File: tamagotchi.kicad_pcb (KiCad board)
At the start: 2 copper layers, 60.8 x 77.1 mm, 10 parts, among them SW1 SW_Push, SW2 SW_Push, SW3 SW_Push, U1 XIAO-ESP32-C3-SMD, U2 HS96L03W2C03

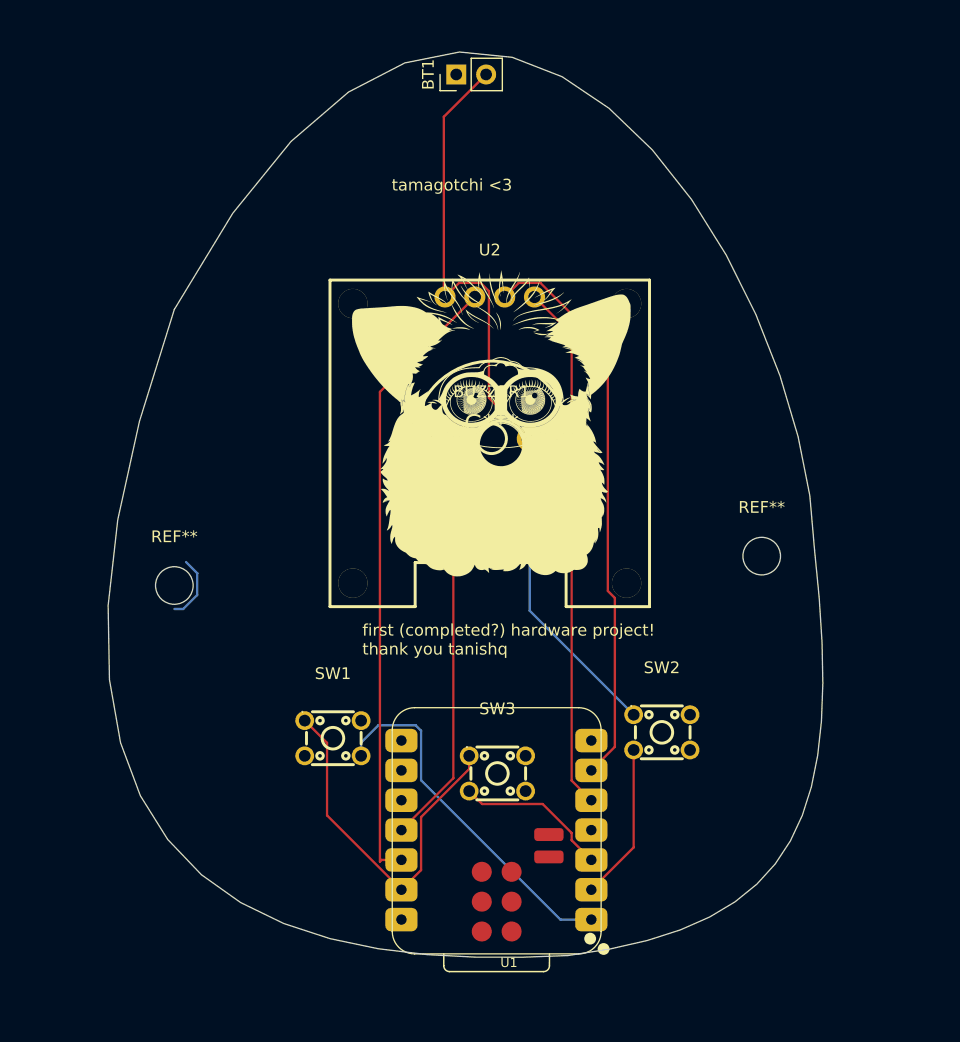
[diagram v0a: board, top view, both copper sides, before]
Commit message: finished routing and fixed DRC errors
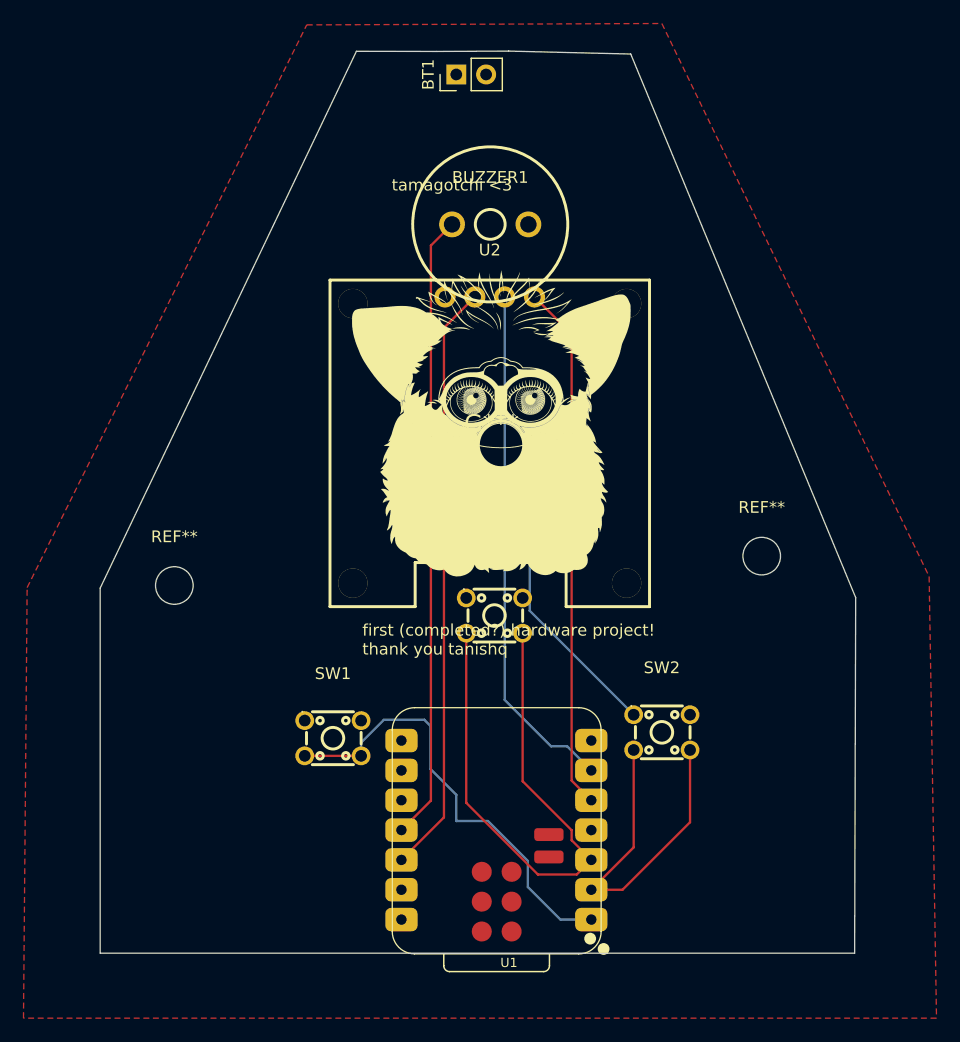
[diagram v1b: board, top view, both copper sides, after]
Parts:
- moved BUZZER1 18.2 mm to (71.9, 54.3)
- moved SW3 13.4 mm to (72.2, 87.6)
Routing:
- net GND: track 97.8 -> 27.3 mm
- net Net-(U1-GPIO4_A2_D2): track 13.2 -> 49.8 mm
- net Net-(BUZZER1-+): track 35.2 -> 53.3 mm
- net Net-(U1-GPIO3_A1_D1): track 13.4 -> 30.3 mm
- net Net-(U1-GPIO2_A0_D0): track 30.7 -> 38.1 mm
- net (no net): track 5.65 -> 0.00 mm
- net Net-(U1-GPIO7_D5_SCL): track 48.5 -> 44.2 mm
- net +3V3: track 53.3 -> 50.5 mm
- added copper zone on F.Cu, net GND
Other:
- board size 60.8 x 77.1 mm -> 64.3 x 76.8 mm

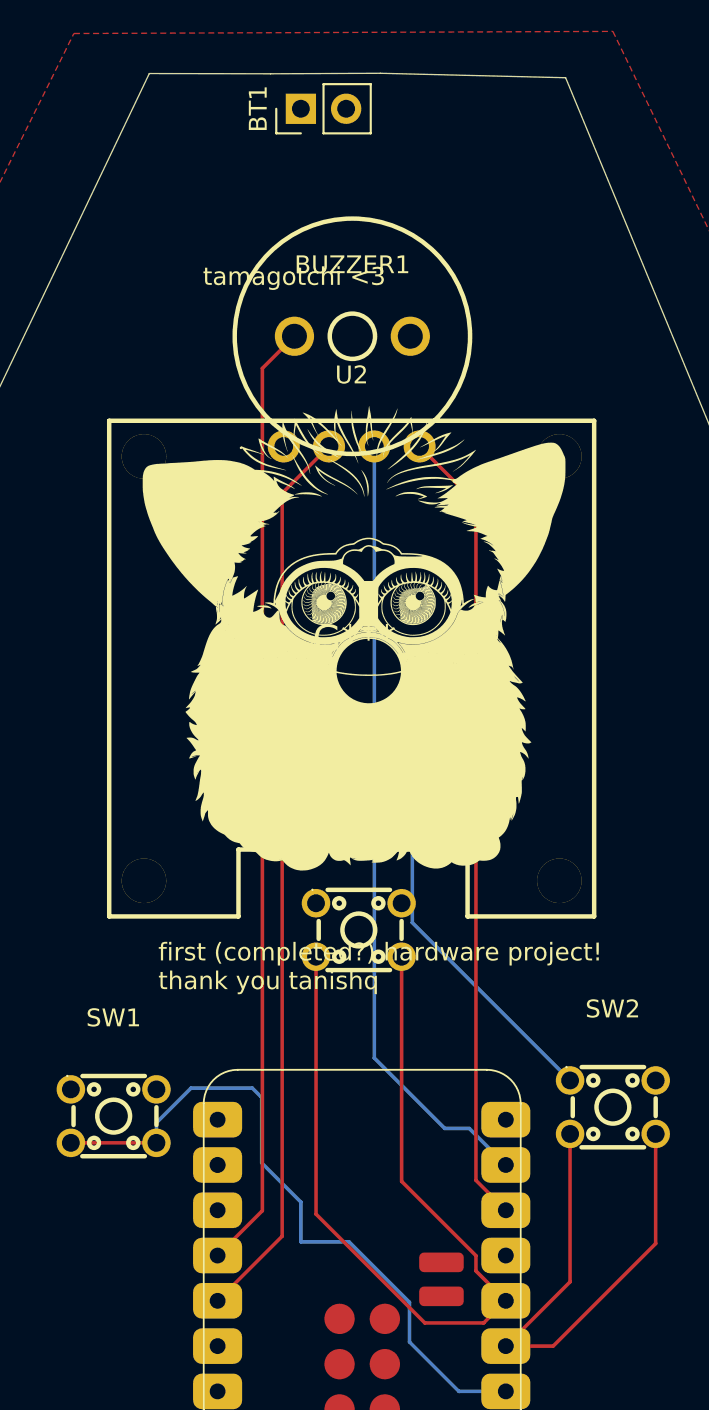
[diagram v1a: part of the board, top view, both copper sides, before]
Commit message: fixed up some really dumb xiao-esp32 issues (namely with the button numbers being wrong
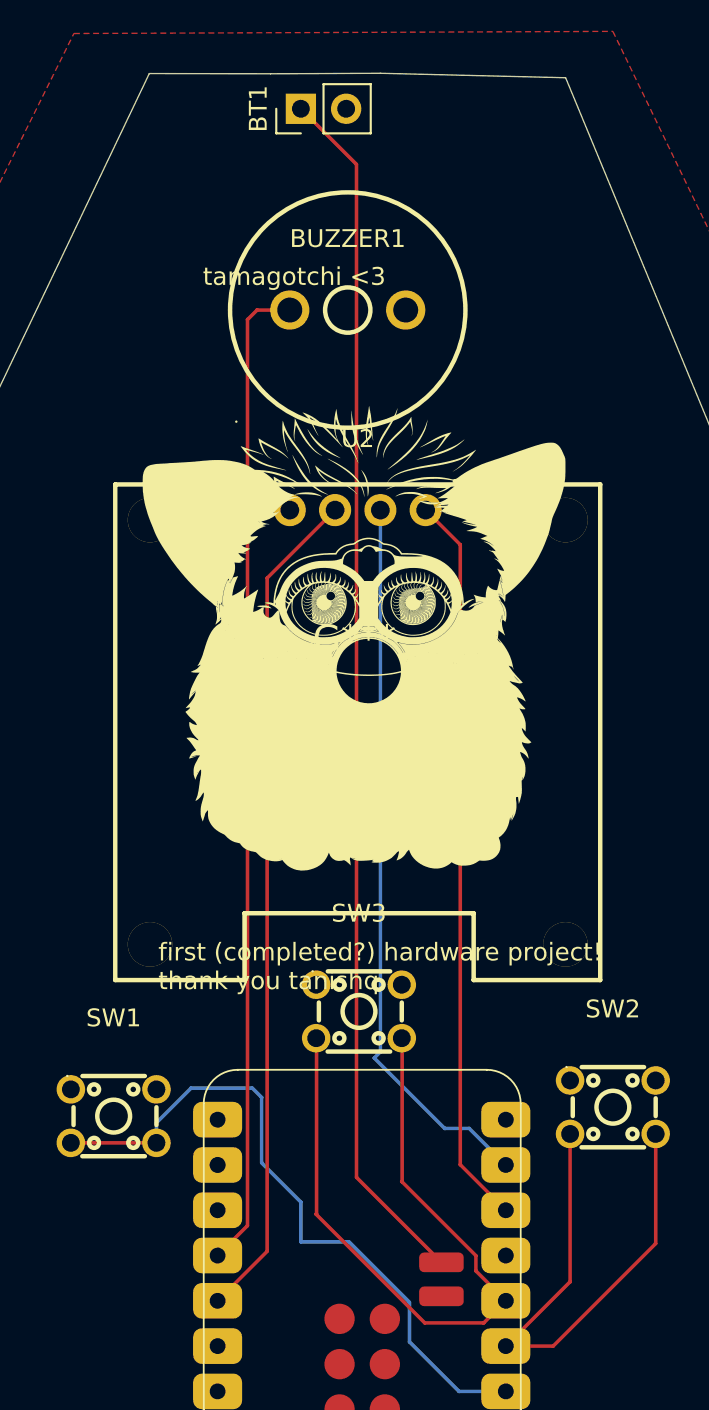
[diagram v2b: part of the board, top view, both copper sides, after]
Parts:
- moved SW3 4.57 mm to (72.3, 92.1)
- moved U2 3.59 mm to (72.2, 64.0)
- moved BUZZER1 1.49 mm to (71.6, 52.8)
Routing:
- net +BATT: track 0.00 -> 68.0 mm
- net GND: track 27.3 -> 0.00 mm
- net Net-(U1-GPIO4_A2_D2): track 49.8 -> 39.6 mm
- net Net-(U1-GPIO6_D4_SDA): track 44.8 -> 41.1 mm
- net Net-(U1-GPIO7_D5_SCL): track 44.2 -> 40.7 mm
- net +3V3: track 50.5 -> 47.1 mm
- net Net-(BUZZER1-+): track 53.3 -> 55.8 mm
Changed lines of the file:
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@@
 			(thermal_bridge_angle 45)
 		)
-		(pad "15" smd roundrect
-			(at 4.445 -10.882)
-			(size 2.5 1.1)
-			(layers "F.Cu" "F.Mask" "F.Paste")
-			(roundrect_rratio 0.25)
-			(thermal_bridge_angle 45)
-		)
-		(pad "16" smd roundrect
-			(at 4.445 -12.787)
-			(size 2.5 1.1)
-			(layers "F.Cu" "F.Mask" "F.Paste")
-			(roundrect_rratio 0.25)
-			(thermal_bridge_angle 45)
-		)
-		(pad "17" smd circle
+		(pad "24" smd circle
 			(at 7.62 -19.132 180)
 			(size 1.7 1.7)
 			(layers "F.Cu" "F.Mask" "F.Paste")
+			(net "unconnected-(U1-GPIO5_MTDI-Pad24)")
+			(pinfunction "GPIO5_MTDI_24")
+			(pintype "passive+no_connect")
 		)
-		(pad "18" smd circle
+		(pad "25" smd circle
 			(at 10.16 -19.132 180)
 			(size 1.7 1.7)
 			(layers "F.Cu" "F.Mask" "F.Paste")
+			(net "unconnected-(U1-GPIO7_MTDO-Pad25)")
+			(pinfunction "GPIO7_MTDO_25")
+			(pintype "passive+no_connect")
 		)
-		(pad "19" smd circle
+		(pad "26" smd circle
 			(at 7.62 -16.592 180)
 			(size 1.7 1.7)
 			(layers "F.Cu" "F.Mask" "F.Paste")
+			(net "unconnected-(U1-CHIP_EN-Pad26)")
+			(pinfunction "CHIP_EN_26")
+			(pintype "passive+no_connect")
 		)
-		(pad "20" smd circle
+		(pad "27" smd circle
 			(at 10.16 -16.592 180)
 			(size 1.7 1.7)
 			(layers "F.Cu" "F.Mask" "F.Paste")
+			(net "unconnected-(U1-GND-Pad27)")
+			(pinfunction "GND_27")
+			(pintype "passive+no_connect")
 		)
-		(pad "21" smd circle
+		(pad "28" smd circle
 			(at 7.62 -14.052 180)
 			(size 1.7 1.7)
 			(layers "F.Cu" "F.Mask" "F.Paste")
+			(net "unconnected-(U1-GPIO4_MTMS-Pad28)")
+			(pinfunction "GPIO4_MTMS_28")
+			(pintype "passive+no_connect")
 		)
-		(pad "22" smd circle
+		(pad "29" smd circle
 			(at 10.16 -14.052 180)
 			(size 1.7 1.7)
 			(layers "F.Cu" "F.Mask" "F.Paste")
+			(net "unconnected-(U1-GPIO6_MTCK-Pad29)")
+			(pinfunction "GPIO6_MTCK_29")
+			(pintype "passive+no_connect")
+		)
+		(pad "32" smd roundrect
+			(at 4.445 -10.882)
+			(size 2.5 1.1)
+			(layers "F.Cu" "F.Mask" "F.Paste")
+			(roundrect_rratio 0.25)
+			(net "+BATT")
+			(pinfunction "BAT_32")
+			(pintype "passive")
+			(thermal_bridge_angle 45)
+		)
+		(pad "33" smd roundrect
+			(at 4.445 -12.787)
+			(size 2.5 1.1)
+			(layers "F.Cu" "F.Mask" "F.Paste")
+			(roundrect_rratio 0.25)
+			(net "GND")
+			(pinfunction "GND_33")
+			(pintype "passive")
+			(thermal_bridge_angle 45)
 		)
 		(embedded_fonts no)
@@
 	(footprint "easyeda2kicad:SW-TH_4P-L4.5-W4.5-P3.00-LS4.8"
 		(layer "F.Cu")
-		(at 72.25 87.56)
+		(at 72.26 92.13)
 		(property "Reference" "SW3"
 			(at 0 -5.5 0)
@@
 	(footprint "easyeda2kicad:BUZ-TH_BD12.5-P6.50-D1.4"
 		(layer "F.Cu")
-		(at 71.89 54.26)
+		(at 71.62946 52.789706)
 		(property "Reference" "BUZZER1"
 			(at 0 -4 0)
@@
 			(layer "F.SilkS")
 		)
-		(fp_line
-			(start -6.25 0)
-			(end 6.25 0)
-			(stroke
-				(width 0.05)
-				(type solid)
-			)
-			(layer "F.CrtYd")
-		)
-		(fp_line
-			(start 6.25 0)
-			(end -6.25 0)
+		(fp_rect
+			(start -9.96025 -7.5435)
+			(end 9.481331 7.524089)
 			(stroke
 				(width 0.05)
-				(type solid)
+				(type default)
 			)
+			(fill no)
 			(layer "F.CrtYd")
 		)
@@
 	(footprint "easyeda2kicad:OLED-TH_L27.8-W27.2-P2.54_C9900033791"
 		(layer "F.Cu")
-		(at 71.85 60.44)
+		(at 72.19 64.01)
 		(property "Reference" "U2"
 			(at 0 -4 0)
@@
 		(layer "Edge.Cuts")
 	)
-	(gr_line
-		(start 66.33 52.03)
-		(end 66.33 55.74)
-		(stroke
-			(width 0.05)
-			(type default)
-		)
-		(layer "F.CrtYd")
-	)
-	(gr_line
-		(start 77.73 55.74)
-		(end 66.33 55.74)
-		(stroke
-			(width 0.05)
-			(type default)
-		)
-		(layer "F.CrtYd")
-	)
-	(gr_line
-		(start 77.73 55.74)
-		(end 77.86 52.09)
-		(stroke
-			(width 0.05)
-			(type default)
-		)
-		(layer "F.CrtYd")
-	)
-	(gr_line
-		(start 77.86 52.09)
-		(end 66.33 52.03)
-		(stroke
-			(width 0.05)
-			(type default)
-		)
-		(layer "F.CrtYd")
-	)
 	(image
 		(at 70.73 72.500001)
@@
 	)
 	(segment
+		(start 74.68 101.69)
+		(end 78.8205 105.8305)
+		(width 0.2)
+		(layer "F.Cu")
+		(net "Net-(U1-GPIO4_A2_D2)")
+	)
+	(segment
 		(start 75.95 109.6)
 		(end 79.25525 109.6)
@@
 	)
 	(segment
+		(start 74.68 94.2)
+		(end 74.68 101.69)
+		(width 0.2)
+		(layer "F.Cu")
+		(net "Net-(U1-GPIO4_A2_D2)")
+	)
+	(segment
 		(start 79.25525 109.6)
 		(end 80.4955 108.35975)
@@
 	)
 	(segment
-		(start 69.85 103.5)
-		(end 75.95 109.6)
+		(start 69.88 103.47)
+		(end 69.85 103.5)
 		(width 0.2)
 		(layer "F.Cu")
@@
 	)
 	(segment
-		(start 74.65 101.66)
-		(end 78.8205 105.8305)
+		(start 69.88 94.2)
+		(end 69.88 103.47)
 		(width 0.2)
 		(layer "F.Cu")
@@
 	)
 	(segment
-		(start 78.8205 106.68475)
-		(end 80.4955 108.35975)
+		(start 69.85 103.5)
+		(end 75.95 109.6)
 		(width 0.2)
 		(layer "F.Cu")
@@
 	)
 	(segment
-		(start 78.8205 105.8305)
-		(end 78.8205 106.68475)
+		(start 74.65 101.66)
+		(end 74.68 101.69)
 		(width 0.2)
 		(layer "F.Cu")
@@
 	)
 	(segment
-		(start 74.65 89.06)
-		(end 74.65 101.66)
+		(start 78.8205 106.68475)
+		(end 80.4955 108.35975)
 		(width 0.2)
 		(layer "F.Cu")
@@
 	)
 	(segment
-		(start 69.85 89.06)
-		(end 69.85 103.5)
+		(start 78.8205 105.8305)
+		(end 78.8205 106.68475)
 		(width 0.2)
 		(layer "F.Cu")
@@
 	)
 	(segment
-		(start 78.8205 63.6005)
-		(end 78.8205 101.60475)
+		(start 76 64.01)
+		(end 77.94 65.95)
 		(width 0.2)
 		(layer "F.Cu")
@@
 	)
 	(segment
-		(start 78.8205 101.60475)
+		(start 77.94 100.72425)
 		(end 80.4955 103.27975)
 		(width 0.2)
@@
 	)
 	(segment
-		(start 75.66 60.44)
-		(end 78.8205 63.6005)
+		(start 77.94 65.95)
+		(end 77.94 100.72425)
 		(width 0.2)
 		(layer "F.Cu")
@@
 	)
 	(segment
+		(start 73.46 94.4)
+		(end 73.12 94.74)
+		(width 0.2)
+		(layer "B.Cu")
+		(net "Net-(U1-GPIO7_D5_SCL)")
+	)
+	(segment
 		(start 80.4955 100.73975)
 		(end 78.44575 98.69)
@@
 	)
 	(segment
-		(start 73.12 94.74)
-		(end 73.12 60.44)
+		(start 73.46 64.01)
+		(end 73.46 94.4)
 		(width 0.2)
 		(layer "B.Cu")
@@
 	)
 	(segment
-		(start 66.84 103.31025)
-		(end 64.3305 105.81975)
+		(start 66.540294 52.789706)
+		(end 66.0055 53.3245)
 		(width 0.2)
 		(layer "F.Cu")
@@
 	)
 	(segment
-		(start 66.84 56.06)
-		(end 66.84 103.31025)
+		(start 66.0055 53.3245)
+		(end 66.0055 104.14475)
 		(width 0.2)
 		(layer "F.Cu")
@@
 	)
 	(segment
-		(start 68.64 54.26)
-		(end 66.84 56.06)
+		(start 68.37946 52.789706)
+		(end 66.540294 52.789706)
 		(width 0.2)
 		(layer "F.Cu")
@@
 	)
 	(segment
-		(start 67.95 63.07)
-		(end 70.58 60.44)
+		(start 66.0055 104.14475)
+		(end 64.3305 105.81975)
+		(width 0.2)
+		(layer "F.Cu")
+		(net "Net-(BUZZER1-+)")
+	)
+	(segment
+		(start 67.11 67.82)
+		(end 70.92 64.01)
 		(width 0.2)
 		(layer "F.Cu")
@@
 	)
 	(segment
-		(start 67.95 104.74025)
-		(end 67.95 63.07)
+		(start 67.11 105.58025)
+		(end 67.11 67.82)
 		(width 0.2)
 		(layer "F.Cu")
@@
 	(segment
 		(start 64.3305 108.35975)
-		(end 67.95 104.74025)
+		(end 67.11 105.58025)
 		(width 0.2)
 		(layer "F.Cu")
@@
 	)
 	(segment
-		(start 68.04 60.44)
-		(end 67.94 60.34)
+		(start 76.8855 106.20175)
+		(end 72.12 101.43625)
 		(width 0.2)
 		(layer "F.Cu")
-		(net "GND")
+		(net "+BATT")
 	)
 	(segment
-		(start 75.25 87.15)
-		(end 75.25 72.5)
+		(start 72.12 101.43625)
+		(end 72.12 44.62)
 		(width 0.2)
-		(layer "B.Cu")
-		(net "GND")
+		(layer "F.Cu")
+		(net "+BATT")
 	)
 	(segment
-		(start 84.1 96)
-		(end 75.25 87.15)
+		(start 72.12 44.62)
+		(end 69 41.5)
 		(width 0.2)
-		(layer "B.Cu")
-		(net "GND")
+		(layer "F.Cu")
+		(net "+BATT")
 	)
 	(zone
